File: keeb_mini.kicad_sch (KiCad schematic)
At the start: 87 parts, among them J1 USB_C_Receptacle_USB2.0_14P, J2 Conn_01x02, SW1 SW_Push, SW10 SW_Push, SW11 SW_Push, SW12 SW_Push, SW13 SW_Push, SW14 SW_Push, SW15 SW_Push, SW16 SW_Push, SW17 SW_Push, SW18 SW_Push, SW19 SW_Push, SW2 SW_Push, SW20 SW_Push, SW21 SW_Push, SW22 SW_Push, SW23 SW_Push, SW24 SW_Push, SW25 SW_Push, SW26 SW_Push, SW27 SW_Push, SW28 SW_Push, SW29 SW_Push, SW3 SW_Push, SW30 SW_Push, SW4 SW_Push, SW5 SW_Push, SW6 SW_Push, SW7 SW_Push, SW8 SW_Push, SW9 SW_Push, U1 NCP1117-3.3_SOT223, U2 RP2040, U3 W25Q128JVS, Y1 Crystal

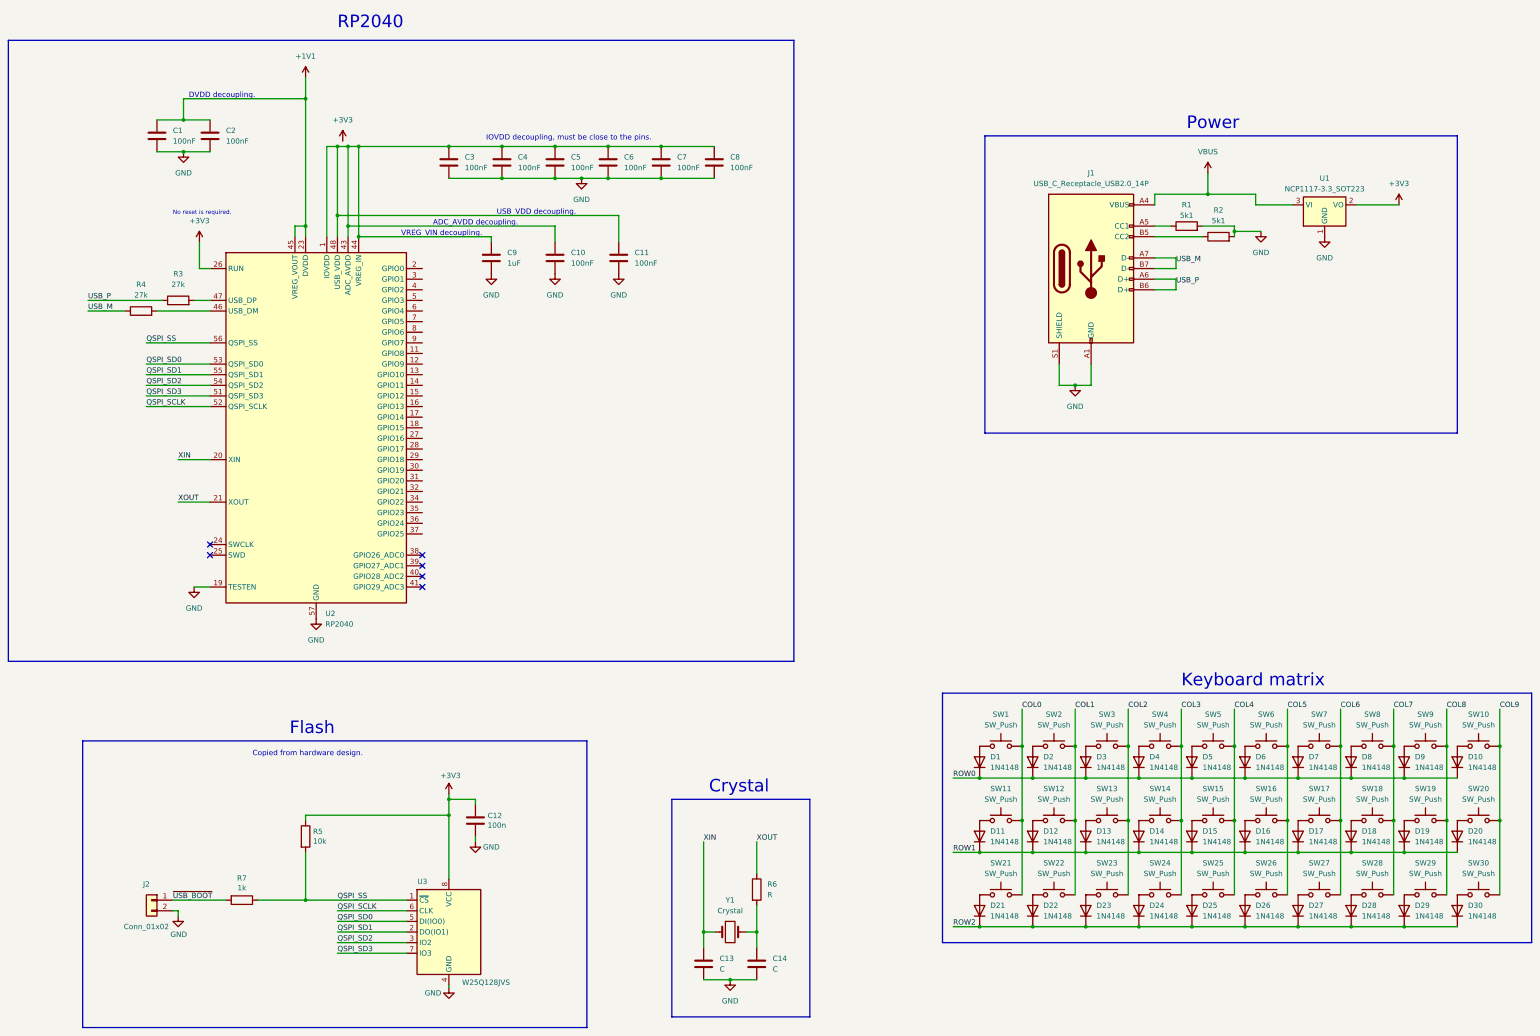
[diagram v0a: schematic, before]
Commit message: Started PCB making, encountered issues with routing
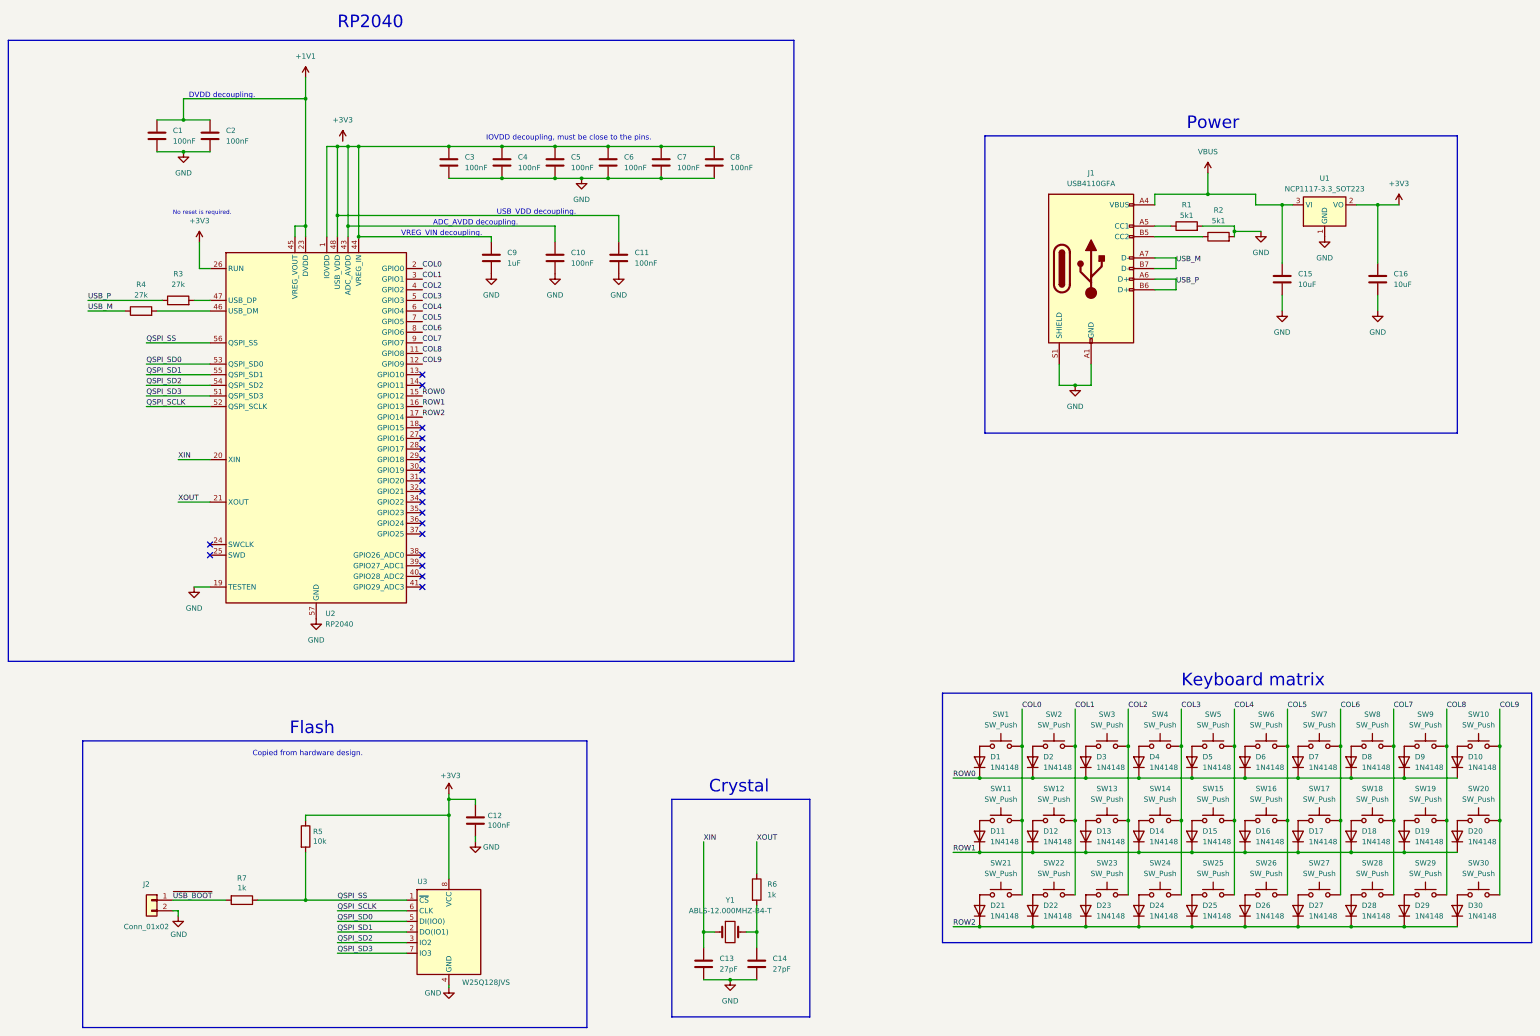
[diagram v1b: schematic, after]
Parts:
- added C15, C16: 10uF, Capacitor_SMD:C_0805_2012Metric, symbol Device:C
- C1, C10, C11, C2, C3, C4, C5, C6, C7, C8, C9: footprint (none) -> Capacitor_SMD:C_0805_2012Metric
- C12: value 100n -> 100nF; footprint Capacitor_SMD:C_0402_1005Metric -> Capacitor_SMD:C_0805_2012Metric
- C13, C14: value C -> 27pF; footprint (none) -> Capacitor_SMD:C_0805_2012Metric
- D1, D10, D11, D12, D13, D14, D15, D16, D17, D18, D19, D2, D20, D21, D22, D23, D24, D25, D26, D27, D28, D29, D3, D30, D4, D5, D6, D7, D8, D9: footprint Diode_THT:D_DO-35_SOD27_P7.62mm_Horizontal -> Diode_SMD:D_SOD-523
- J1: value USB_C_Receptacle_USB2.0_14P -> USB4110GFA; footprint (none) -> Connector_USB:USB_C_Receptacle_GCT_USB4110
- R1, R2, R3, R4: footprint (none) -> Resistor_SMD:R_0805_2012Metric
- R5, R7: footprint Resistor_SMD:R_0402_1005Metric -> Resistor_SMD:R_0805_2012Metric
- R6: value R -> 1k; footprint (none) -> Resistor_SMD:R_0805_2012Metric
- Y1: value Crystal -> ABLS-12.000MHZ-B4-T; footprint (none) -> Crystal:Crystal_SMD_HC49-SD
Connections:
- net +3V3: now also C16.1
- net COL0: now also U2.2 (GPIO0)
- net COL1: now also U2.3 (GPIO1)
- net COL2: now also U2.4 (GPIO2)
- net COL3: now also U2.5 (GPIO3)
- net COL4: now also U2.6 (GPIO4)
- net COL5: now also U2.7 (GPIO5)
- net COL6: now also U2.8 (GPIO6)
- net COL7: now also U2.9 (GPIO7)
- net COL8: now also U2.11 (GPIO8)
- net COL9: now also U2.12 (GPIO9)
- net GND: now also C15.2, C16.2
- net ROW0: now also U2.15 (GPIO12)
- net ROW1: now also U2.16 (GPIO13)
- net ROW2: now also U2.17 (GPIO14)
- net VBUS: now also C15.1
- no-connect marks 6 -> 19
